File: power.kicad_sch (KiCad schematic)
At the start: 35 parts, among them IC302 L7805, IC303 L7805, P302 POWER, Q503 BR 29, SW101 SW_SPDT

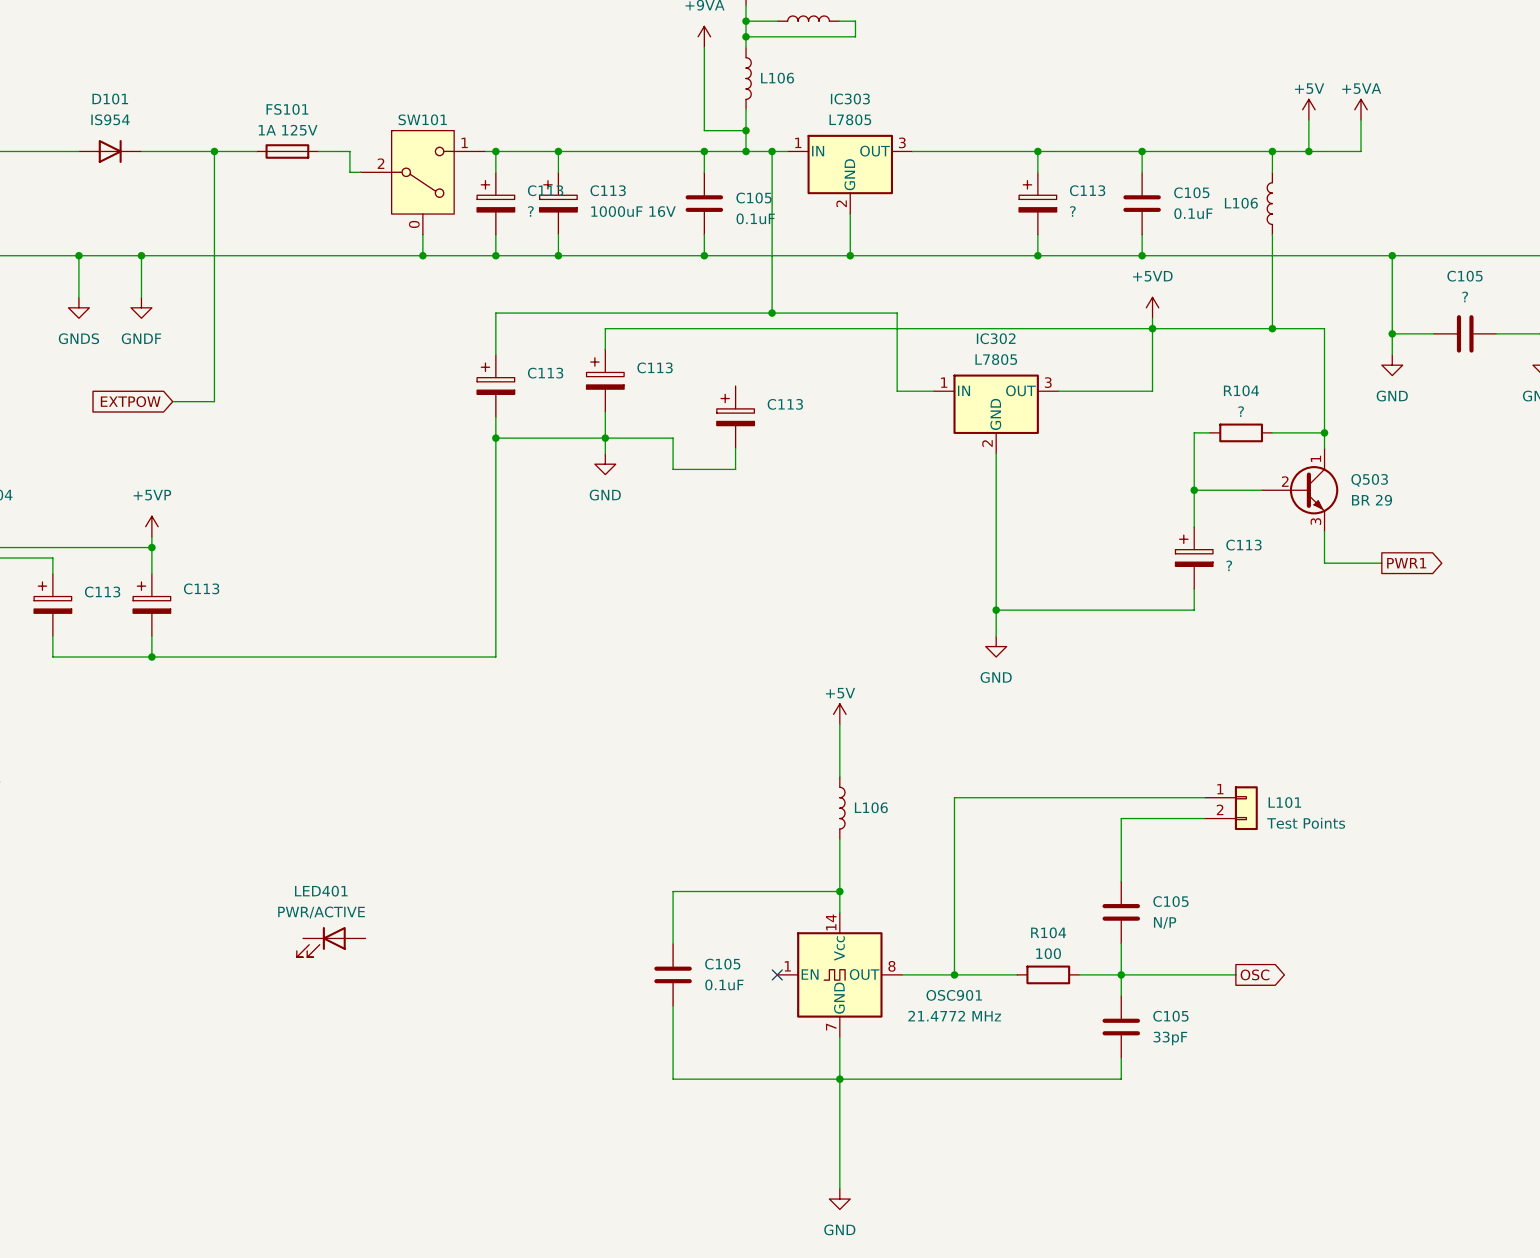
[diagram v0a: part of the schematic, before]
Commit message: More passives on back.
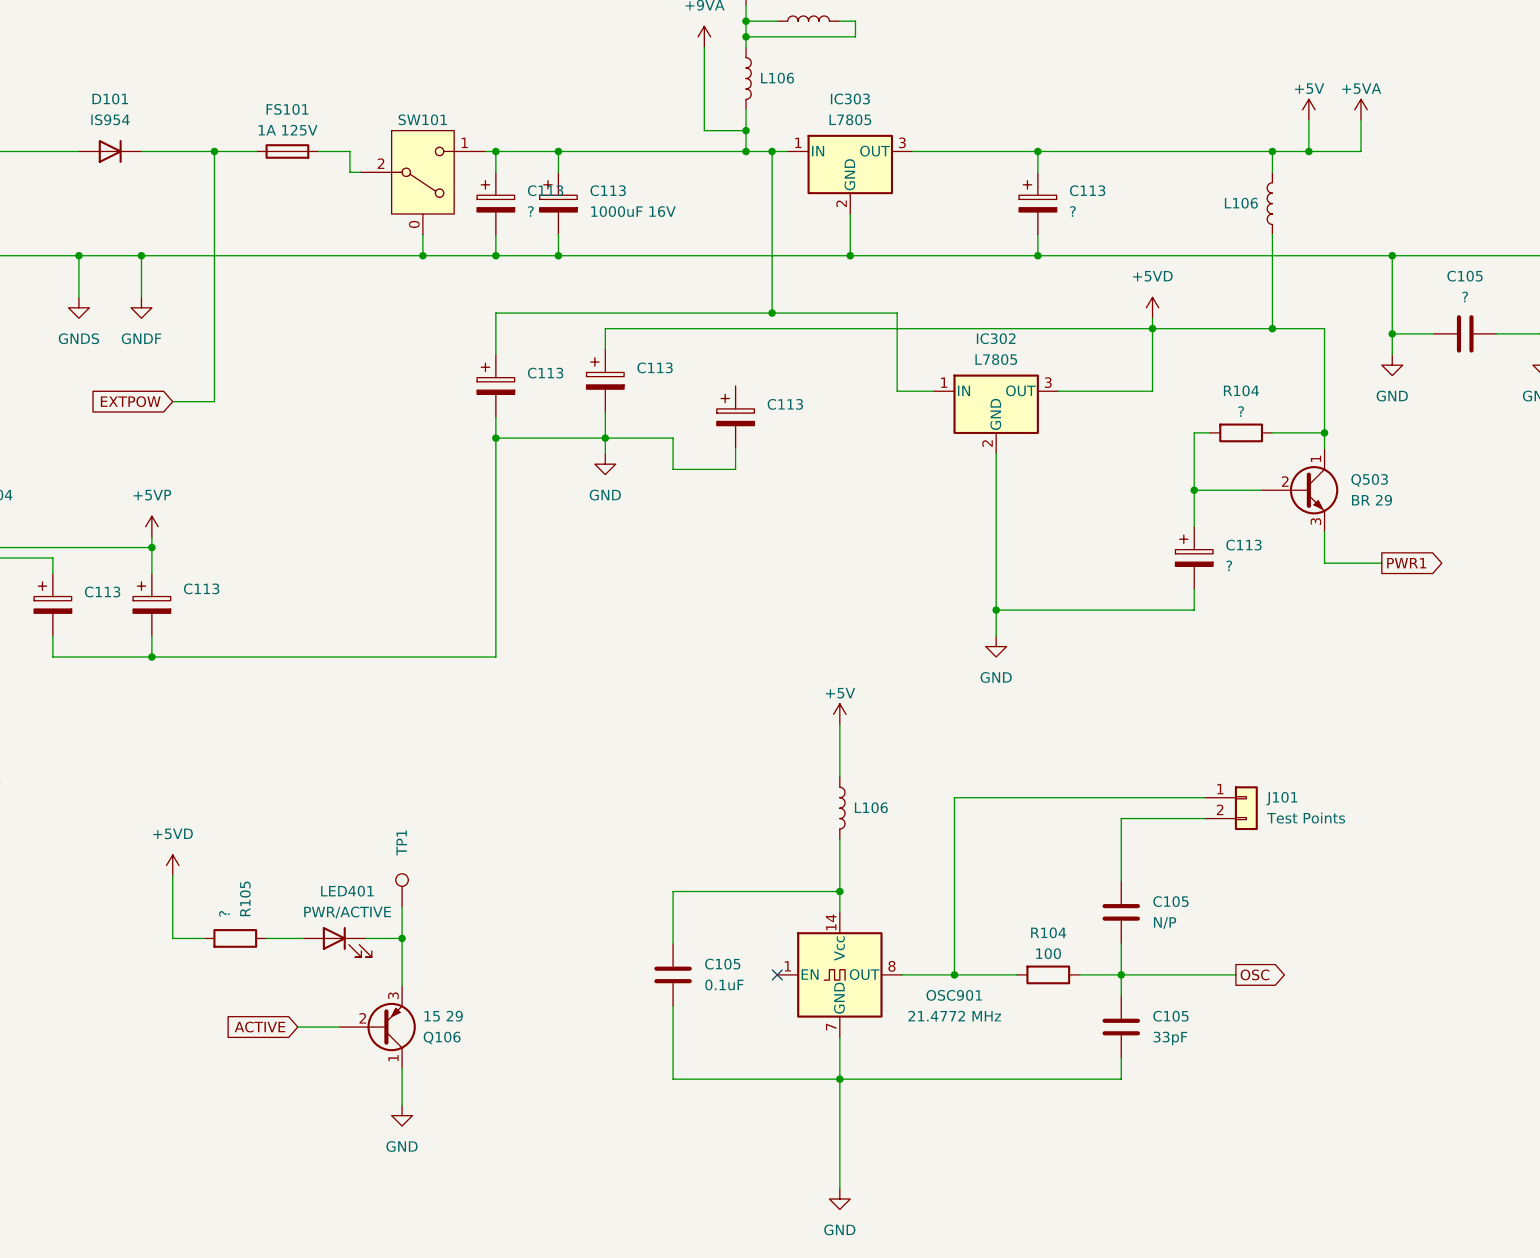
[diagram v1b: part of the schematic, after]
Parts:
- removed C105 (x2): 0.1uF, A-PCENGINE:SMD_0805_Narrow, symbol Device:C
- added Q106: 15 29, A-PCENGINE:Transistor_SMD, symbol Device:Q_PNP_CBE
- added R105: ?, A-PCENGINE:SMD_1210, symbol Device:R
- added TP1: ~, A-PCENGINE:Test_Point_1.5mm, symbol Connector:TestPoint
- renumbered L101 to J101
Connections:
- net +5VD: now also R105.2
- net GND: now also Q106.1 (C)
- net at LED401.1 (K): now also Q106.3 (E), TP1.1
- net at LED401.2 (A): now also R105.1
- new net ACTIVE: Q106.2 (B)
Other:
- moved on the sheet: LED401

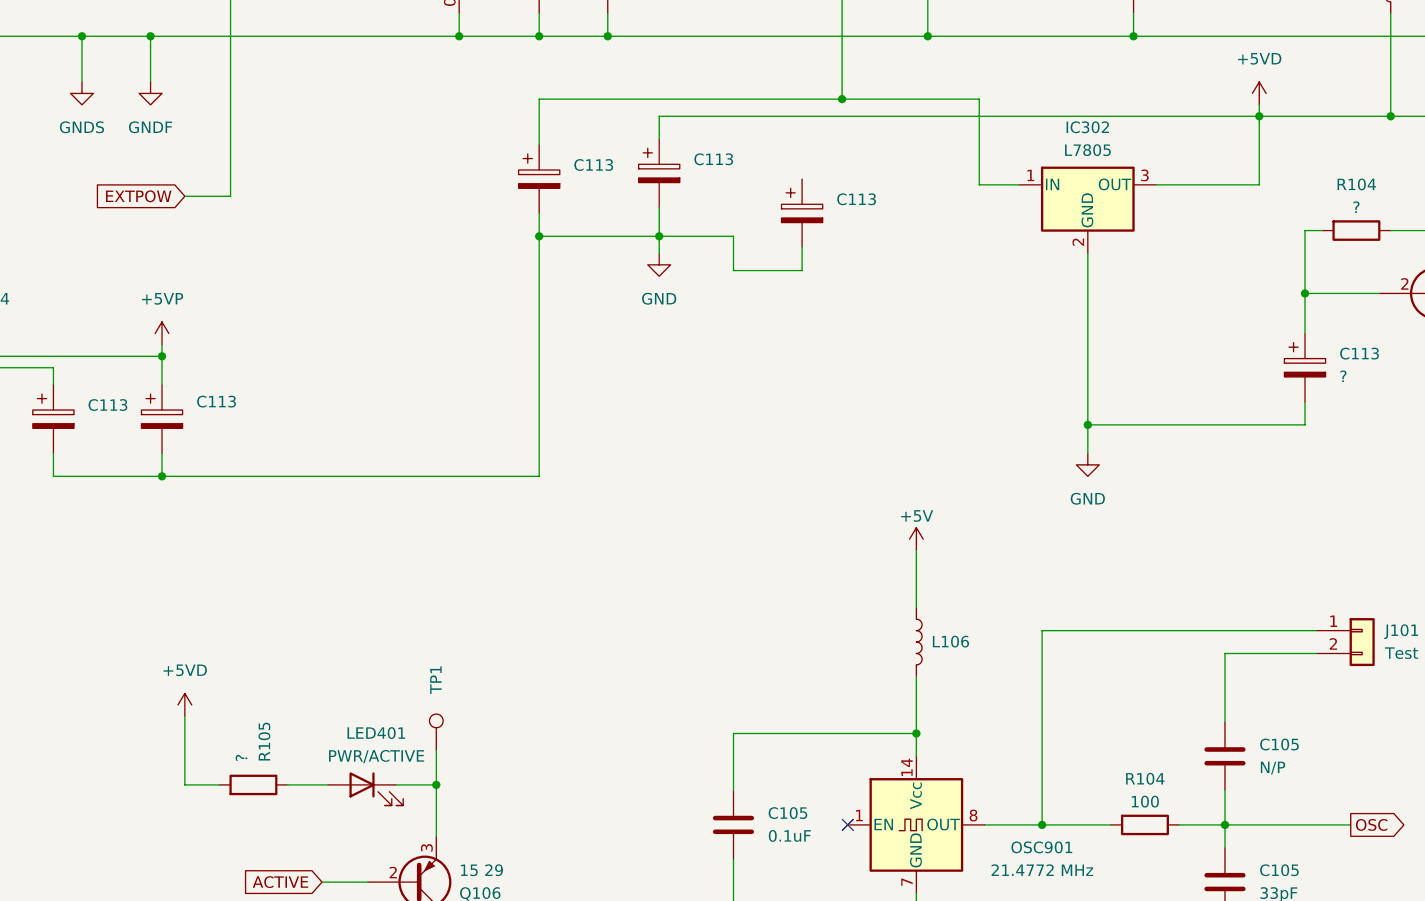
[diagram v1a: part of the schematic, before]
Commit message: Yet more passives on back.
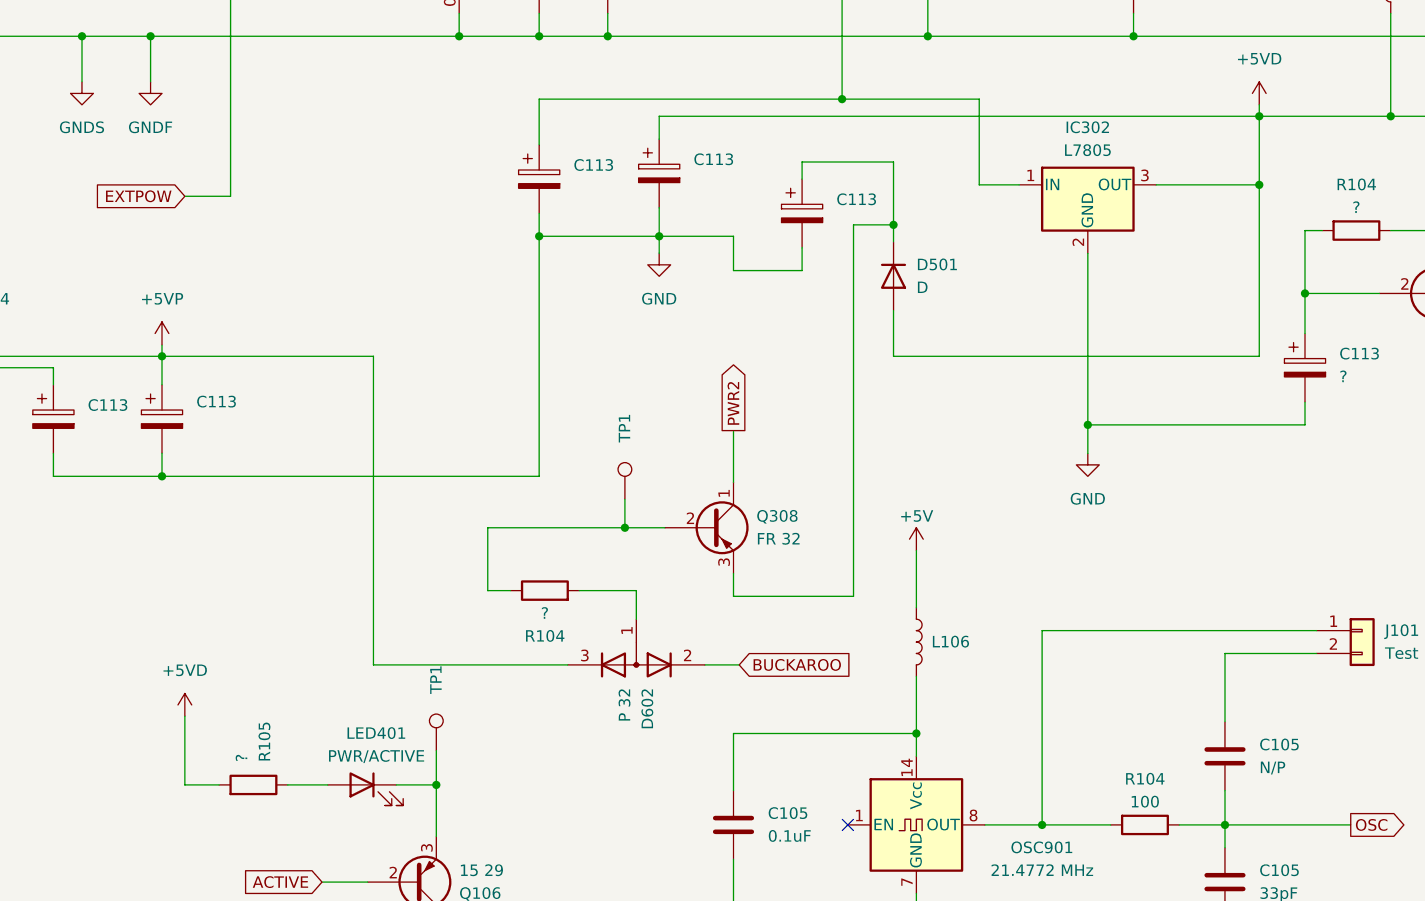
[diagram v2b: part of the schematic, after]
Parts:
- added D501: D, A-PCENGINE:Transistor_SMD, symbol Device:D
- added D602: P 32, A-PCENGINE:Transistor_SMD, symbol Device:D_Dual_CommonAnode_AKK
- added Q308: FR 32, A-PCENGINE:Transistor_SMD, symbol Device:Q_PNP_CBE
- added R104: ?, A-PCENGINE:SMD_0805_Narrow_Long, symbol Device:R
- added TP1: ~, A-PCENGINE:Test_Point_1.5mm, symbol Connector:TestPoint
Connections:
- net +5VD: now also D501.2 (A)
- net +5VP: now also D602.3 (K)
- net at C113.1: now also D501.1 (K), Q308.3 (E)
- new net: Q308.2 (B), R104.1, TP1.1
- new net: D602.1 (A), R104.2
- new net BUCKAROO: D602.2 (K)
- new net PWR2: Q308.1 (C)

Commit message: First draft complete.
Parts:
- added R105: ?, A-PCENGINE:SMD_1210, symbol Device:R
- added TP40: ~, A-PCENGINE:Test_Point_1.5mm, symbol Connector:TestPoint
- added ZD302: D_Zener, A-PCENGINE:Transistor_SMD, symbol Device:D_Zener
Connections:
- net +5VP: now also TP40.1
- net +9VA: now also R105.2
- net GND: now also ZD302.2 (A)
- net at C113.1, Q304.2 (B): now also R105.1, ZD302.1 (K)
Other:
- moved on the sheet: C113, LED401, Q106, R105, TP1

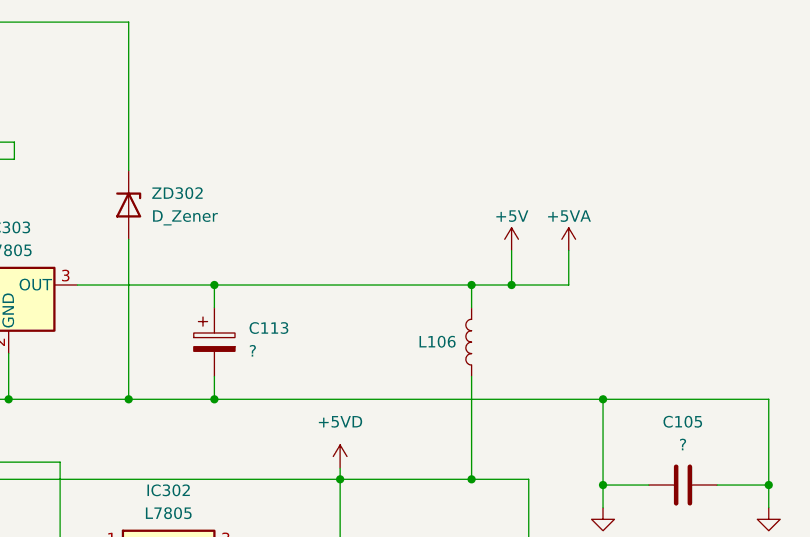
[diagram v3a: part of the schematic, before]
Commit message: Fix DRC errors.
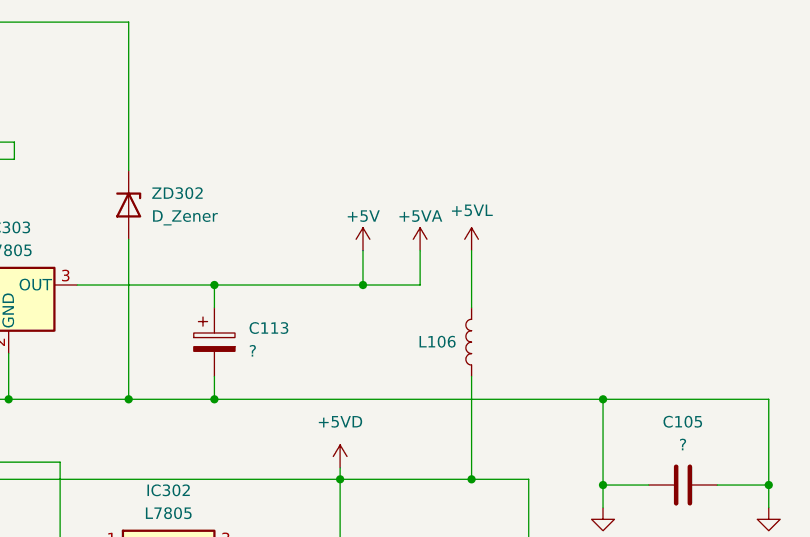
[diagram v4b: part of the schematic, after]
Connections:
- net +5V: no longer L106.2
- new net +5VL: L106.2
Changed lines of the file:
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@@
   (junction (at 289.56 72.39) (diameter 0) (color 0 0 0 0)
   )
+  (junction (at 292.1 50.8) (diameter 0) (color 0 0 0 0)
+  )
   (junction (at 175.26 50.8) (diameter 0) (color 0 0 0 0)
   )
-  (junction (at 304.165 50.8) (diameter 0) (color 0 0 0 0)
-  )
   (junction (at 147.32 144.78) (diameter 0) (color 0 0 0 0)
   )
@@
   )
   (junction (at 318.77 73.025) (diameter 0) (color 0 0 0 0)
-  )
-  (junction (at 308.61 50.8) (diameter 0) (color 0 0 0 0)
   )
   (junction (at 147.32 158.75) (diameter 0) (color 0 0 0 0)
@@
     (stroke (width 0) (type default))
   )
-  (wire (pts (xy 314.96 50.8) (xy 314.96 46.99))
+  (wire (pts (xy 298.45 50.8) (xy 298.45 46.99))
     (stroke (width 0) (type default))
   )
@@
     (stroke (width 0) (type default))
   )
-  (wire (pts (xy 275.59 50.8) (xy 304.165 50.8))
-    (stroke (width 0) (type default))
-  )
   (wire (pts (xy 259.08 151.13) (xy 265.43 151.13))
     (stroke (width 0) (type default))
@@
     (stroke (width 0) (type default))
   )
-  (wire (pts (xy 308.61 50.8) (xy 314.96 50.8))
-    (stroke (width 0) (type default))
-  )
   (wire (pts (xy 209.55 85.725) (xy 222.885 85.725))
     (stroke (width 0) (type default))
@@
     (stroke (width 0) (type default))
   )
+  (wire (pts (xy 304.165 46.99) (xy 304.165 53.34))
+    (stroke (width 0) (type default))
+  )
   (wire (pts (xy 275.59 63.5) (xy 318.77 63.5))
     (stroke (width 0) (type default))
@@
     (stroke (width 0) (type default))
   )
-  (wire (pts (xy 308.61 50.8) (xy 308.61 46.99))
+  (wire (pts (xy 292.1 50.8) (xy 292.1 46.99))
     (stroke (width 0) (type default))
   )
@@
     (stroke (width 0) (type default))
   )
+  (wire (pts (xy 292.1 50.8) (xy 298.45 50.8))
+    (stroke (width 0) (type default))
+  )
   (wire (pts (xy 280.67 151.13) (xy 285.75 151.13))
     (stroke (width 0) (type default))
@@
     (stroke (width 0) (type default))
   )
-  (wire (pts (xy 304.165 50.8) (xy 308.61 50.8))
+  (wire (pts (xy 275.59 50.8) (xy 292.1 50.8))
     (stroke (width 0) (type default))
   )
@@
   )
   (wire (pts (xy 208.28 50.8) (xy 209.55 50.8))
-    (stroke (width 0) (type default))
-  )
-  (wire (pts (xy 304.165 50.8) (xy 304.165 53.34))
     (stroke (width 0) (type default))
   )
@@
         (path "/c1c718c6-a427-431e-a18b-e46f94ae8e09/ba362b1f-3cb7-4861-9385-2b05dca17551"
           (reference "#PWR054") (unit 1)
+        )
+      )
+    )
+  )
+  (symbol (lib_id "power:+5VL") (at 304.165 46.99 0) (unit 1)
+    (in_bom yes) (on_board yes) (dnp no) (fields_autoplaced)
+    (property "Reference" "#PWR0197" (at 304.165 50.8 0)
+      (effects (font (size 1.27 1.27)) hide)
+    )
+    (property "Value" "+5VL" (at 304.165 42.545 0)
+      (effects (font (size 1.27 1.27)))
+    )
+    (property "Footprint" "" (at 304.165 46.99 0)
+      (effects (font (size 1.27 1.27)) hide)
+    )
+    (property "Datasheet" "" (at 304.165 46.99 0)
+      (effects (font (size 1.27 1.27)) hide)
+    )
+    (pin "1")
+    (instances
+      (project "PCE"
+        (path "/c1c718c6-a427-431e-a18b-e46f94ae8e09/f2e7b294-149a-4ec9-8398-41569f37f2ee"
+          (reference "#PWR0197") (unit 1)
+        )
+        (path "/c1c718c6-a427-431e-a18b-e46f94ae8e09/bec74ead-fbfd-4adb-94cc-b39bf0f8c080"
+          (reference "#PWR0199") (unit 1)
+        )
+        (path "/c1c718c6-a427-431e-a18b-e46f94ae8e09/ba362b1f-3cb7-4861-9385-2b05dca17551"
+          (reference "#PWR087") (unit 1)
         )
       )
@@
     )
   )
-  (symbol (lib_id "power:+5V") (at 308.61 46.99 0) (unit 1)
-    (in_bom yes) (on_board yes) (dnp no) (fields_autoplaced)
-    (property "Reference" "#PWR026" (at 308.61 50.8 0)
-      (effects (font (size 1.27 1.27)) hide)
-    )
-    (property "Value" "+5V" (at 308.61 43.18 0)
-      (effects (font (size 1.27 1.27)))
-    )
-    (property "Footprint" "" (at 308.61 46.99 0)
-      (effects (font (size 1.27 1.27)) hide)
-    )
-    (property "Datasheet" "" (at 308.61 46.99 0)
+  (symbol (lib_id "power:+5V") (at 292.1 46.99 0) (unit 1)
+    (in_bom yes) (on_board yes) (dnp no) (fields_autoplaced)
+    (property "Reference" "#PWR026" (at 292.1 50.8 0)
+      (effects (font (size 1.27 1.27)) hide)
+    )
+    (property "Value" "+5V" (at 292.1 43.18 0)
+      (effects (font (size 1.27 1.27)))
+    )
+    (property "Footprint" "" (at 292.1 46.99 0)
+      (effects (font (size 1.27 1.27)) hide)
+    )
+    (property "Datasheet" "" (at 292.1 46.99 0)
       (effects (font (size 1.27 1.27)) hide)
     )
@@
     )
   )
-  (symbol (lib_id "power:+5VA") (at 314.96 46.99 0) (unit 1)
-    (in_bom yes) (on_board yes) (dnp no) (fields_autoplaced)
-    (property "Reference" "#PWR024" (at 314.96 50.8 0)
-      (effects (font (size 1.27 1.27)) hide)
-    )
-    (property "Value" "+5VA" (at 314.96 43.18 0)
-      (effects (font (size 1.27 1.27)))
-    )
-    (property "Footprint" "" (at 314.96 46.99 0)
-      (effects (font (size 1.27 1.27)) hide)
-    )
-    (property "Datasheet" "" (at 314.96 46.99 0)
-      (effects (font (size 1.27 1.27)) hide)
-    )
+  (symbol (lib_id "power:+5VA") (at 298.45 46.99 0) (unit 1)
+    (in_bom yes) (on_board yes) (dnp no) (fields_autoplaced)
+    (property "Reference" "#PWR024" (at 298.45 50.8 0)
+      (effects (font (size 1.27 1.27)) hide)
+    )
+    (property "Value" "+5VA" (at 298.45 43.18 0)
+      (effects (font (size 1.27 1.27)))
+    )
+    (property "Footprint" "" (at 298.45 46.99 0)
+      (effects (font (size 1.27 1.27)) hide)
+    )
+    (property "Datasheet" "" (at 298.45 46.99 0)
+      (effects (font (size 1.27 1.27)) hide)
+    )
